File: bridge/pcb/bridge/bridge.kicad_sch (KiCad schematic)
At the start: 17 parts, among them J1 Screw_Terminal_01x06, J10 12V_Enable, J2 Screw_Terminal_01x06, J3 Screw_Terminal_01x06, J4 Conn_01x23, SW1 SW_SPST, U2 J104D2C12VDC.20S

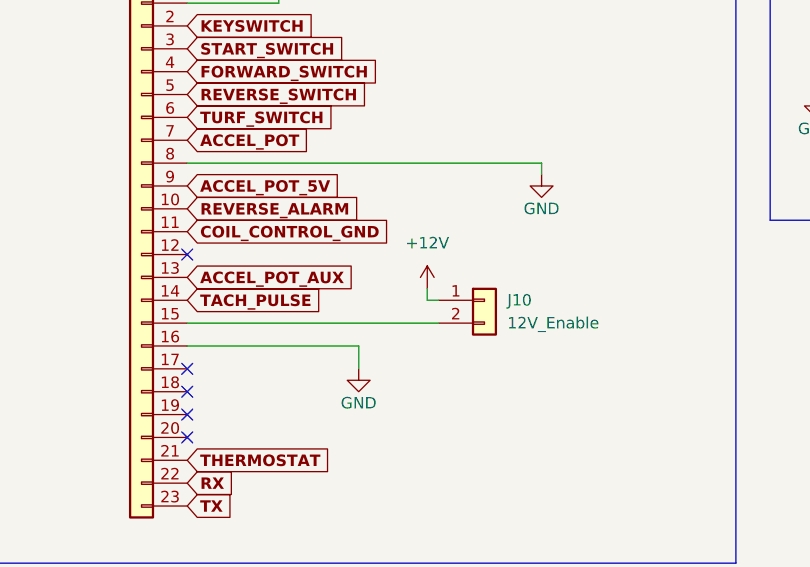
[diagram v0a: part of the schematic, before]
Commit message: Assigned footprints and layed out board
Removed 5V and 12V enable headers as they added unneeded complexity
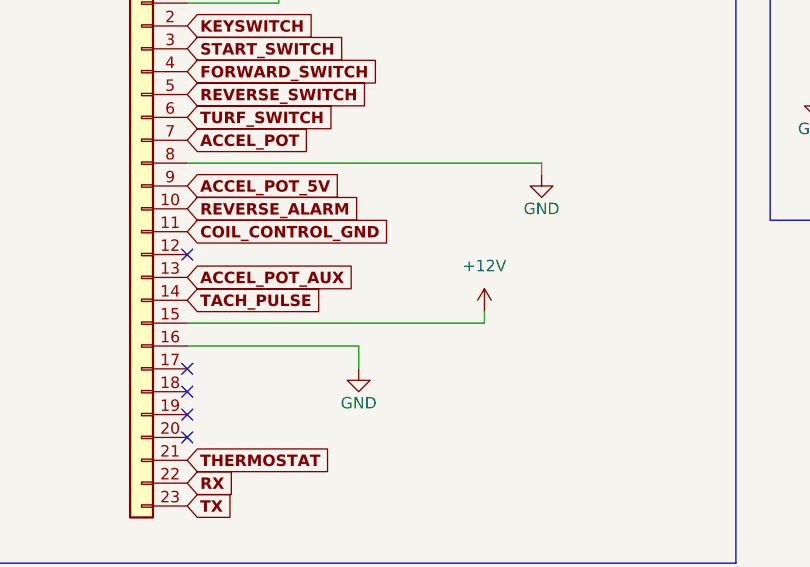
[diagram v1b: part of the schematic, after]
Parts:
- removed J10: 12V_Enable, Connector_PinHeader_2.54mm:PinHeader_1x02_P2.54mm_Vertical, symbol Connector_Generic:Conn_01x02
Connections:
- net +12V: now also J4.15 (Pin_15)
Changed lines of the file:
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@@
     (stroke (width 0) (type default))
   )
-  (wire (pts (xy 41.91 73.66) (xy 69.85 73.66))
+  (wire (pts (xy 41.91 73.66) (xy 74.93 73.66))
     (stroke (width 0) (type default))
   )
@@
     (stroke (width 0) (type default))
   )
+  (wire (pts (xy 74.93 73.66) (xy 74.93 72.39))
+    (stroke (width 0) (type default))
+  )
   (wire (pts (xy 110.49 144.78) (xy 110.49 146.05))
     (stroke (width 0) (type default))
@@
     (stroke (width 0) (type default))
   )
-  (wire (pts (xy 68.58 69.85) (xy 68.58 71.12))
-    (stroke (width 0) (type default))
-  )
   (wire (pts (xy 207.01 106.68) (xy 226.06 106.68))
     (stroke (width 0) (type default))
@@
   )
   (wire (pts (xy 153.67 91.44) (xy 153.67 93.98))
-    (stroke (width 0) (type default))
-  )
-  (wire (pts (xy 68.58 71.12) (xy 69.85 71.12))
     (stroke (width 0) (type default))
   )
@@
     )
   )
-  (symbol (lib_id "Connector_Generic:Conn_01x02") (at 74.93 71.12 0) (unit 1)
-    (in_bom yes) (on_board yes) (dnp no) (fields_autoplaced)
-    (property "Reference" "J10" (at 77.47 71.12 0)
-      (effects (font (size 1.27 1.27)) (justify left))
-    )
-    (property "Value" "12V_Enable" (at 77.47 73.66 0)
-      (effects (font (size 1.27 1.27)) (justify left))
-    )
-    (property "Footprint" "Connector_PinHeader_2.54mm:PinHeader_1x02_P2.54mm_Vertical" (at 74.93 71.12 0)
-      (effects (font (size 1.27 1.27)) hide)
-    )
-    (property "Datasheet" "~" (at 74.93 71.12 0)
-      (effects (font (size 1.27 1.27)) hide)
-    )
-    (pin "1")
-    (pin "2")
-    (instances
-      (project "bridge"
-        (path "/40a0f45e-7290-47b9-8da3-09f7dfbfbbd7"
-          (reference "J10") (unit 1)
-        )
-      )
-    )
-  )
   (symbol (lib_id "Connector:Screw_Terminal_01x06") (at 233.68 109.22 0) (unit 1)
     (in_bom yes) (on_board yes) (dnp no) (fields_autoplaced)
@@
     )
   )
-  (symbol (lib_id "power:+12V") (at 68.58 69.85 0) (unit 1)
-    (in_bom yes) (on_board yes) (dnp no) (fields_autoplaced)
-    (property "Reference" "#PWR03" (at 68.58 73.66 0)
-      (effects (font (size 1.27 1.27)) hide)
-    )
-    (property "Value" "+12V" (at 68.58 64.77 0)
-      (effects (font (size 1.27 1.27)))
-    )
-    (property "Footprint" "" (at 68.58 69.85 0)
-      (effects (font (size 1.27 1.27)) hide)
-    )
-    (property "Datasheet" "" (at 68.58 69.85 0)
-      (effects (font (size 1.27 1.27)) hide)
-    )
+  (symbol (lib_id "power:+12V") (at 74.93 72.39 0) (unit 1)
+    (in_bom yes) (on_board yes) (dnp no) (fields_autoplaced)
+    (property "Reference" "#PWR03" (at 74.93 76.2 0)
+      (effects (font (size 1.27 1.27)) hide)
+    )
+    (property "Value" "+12V" (at 74.93 67.31 0)
+      (effects (font (size 1.27 1.27)))
+    )
+    (property "Footprint" "" (at 74.93 72.39 0)
+      (effects (font (size 1.27 1.27)) hide)
+    )
+    (property "Datasheet" "" (at 74.93 72.39 0)
+      (effects (font (size 1.27 1.27)) hide)
+    )

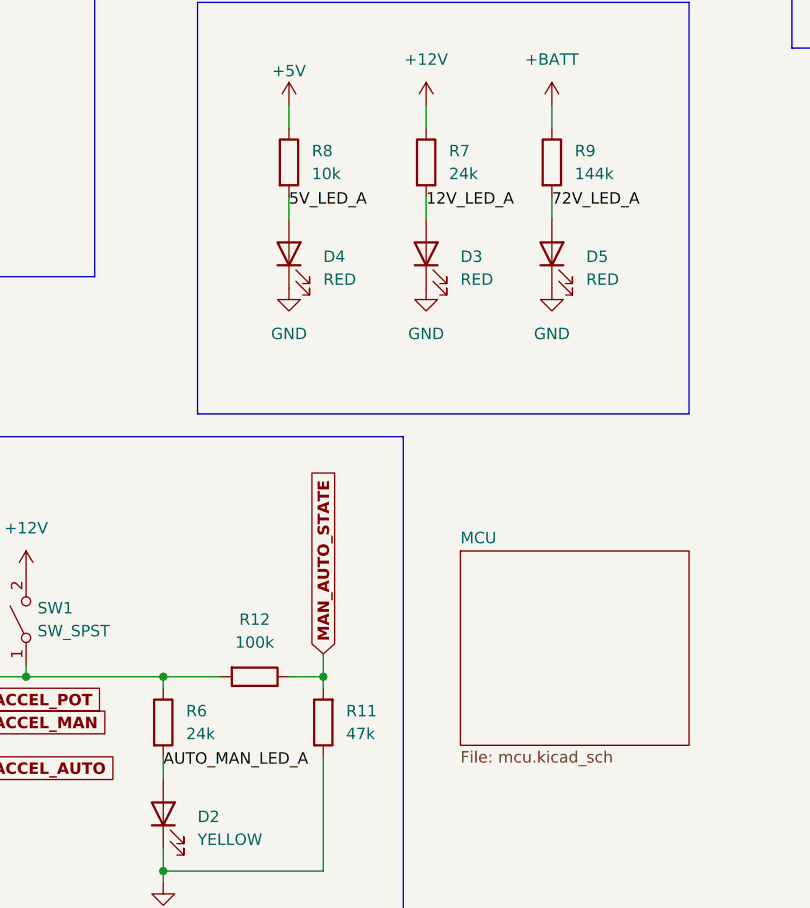
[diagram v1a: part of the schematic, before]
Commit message: Updated resistor values to make LEDs brighter
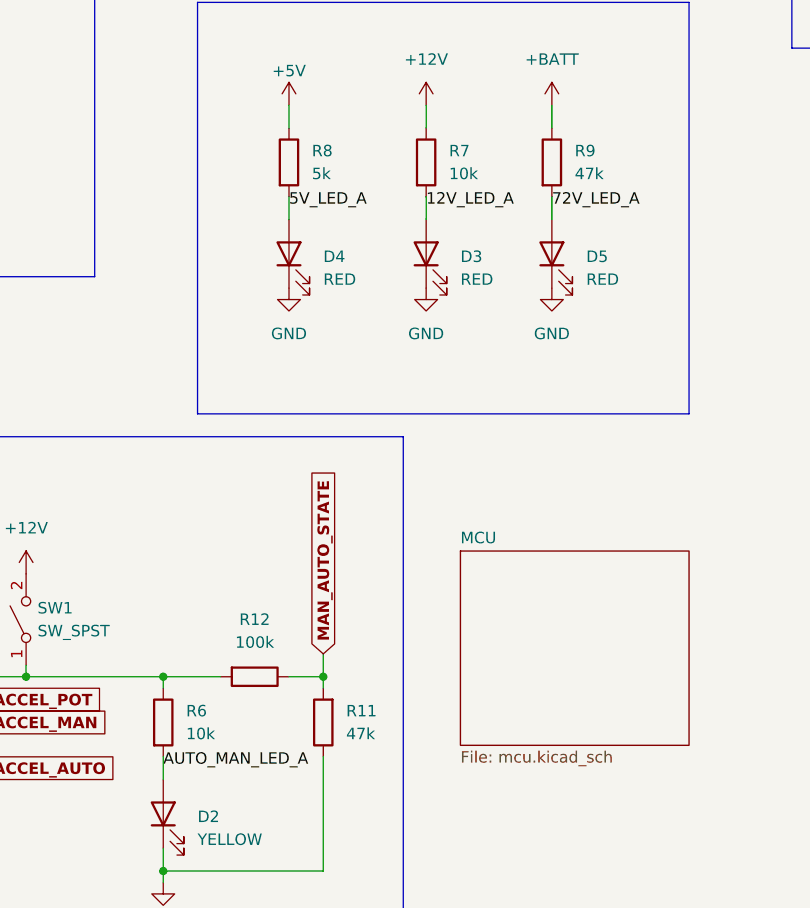
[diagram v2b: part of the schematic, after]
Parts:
- R6, R7: value 24k -> 10k
- R8: value 10k -> 5k
- R9: value 144k -> 47k
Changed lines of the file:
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@@
       (effects (font (size 1.27 1.27)) (justify left))
     )
-    (property "Value" "144k" (at 156.21 88.9 0)
+    (property "Value" "47k" (at 156.21 88.9 0)
       (effects (font (size 1.27 1.27)) (justify left))
     )
@@
       (effects (font (size 1.27 1.27)) (justify left))
     )
-    (property "Value" "10k" (at 127 88.9 0)
+    (property "Value" "5k" (at 127 88.9 0)
       (effects (font (size 1.27 1.27)) (justify left))
     )
@@
       (effects (font (size 1.27 1.27)) (justify left))
     )
-    (property "Value" "24k" (at 142.24 88.9 0)
+    (property "Value" "10k" (at 142.24 88.9 0)
       (effects (font (size 1.27 1.27)) (justify left))
     )
@@
       (effects (font (size 1.27 1.27)) (justify left))
     )
-    (property "Value" "24k" (at 113.03 151.13 0)
-      (effects (font (size 1.27 1.27)) (justify left))
-    )
+    (property "Value" "10k" (at 113.03 151.13 0)
+      (effects (font (size 1.27 1.27)) (justify left))
+    )

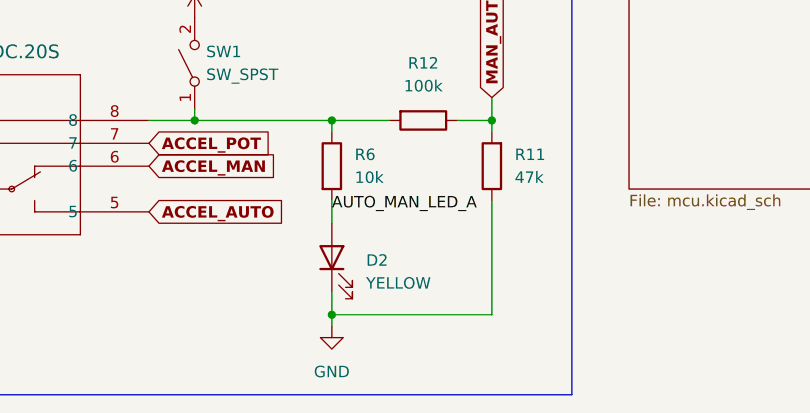
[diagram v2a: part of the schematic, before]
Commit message: Adjusted LED colors
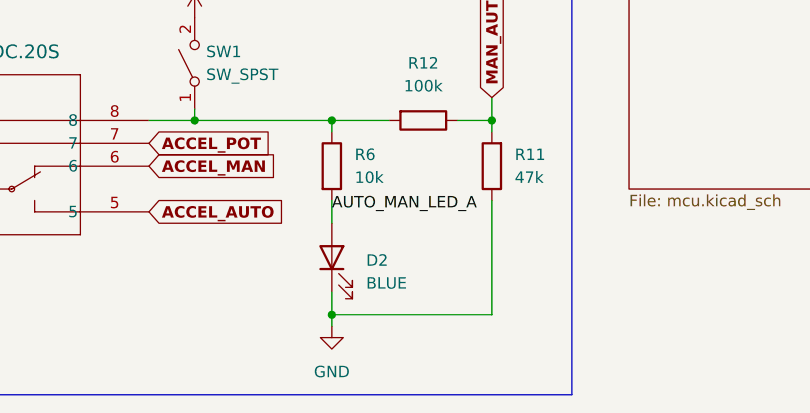
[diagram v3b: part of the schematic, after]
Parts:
- D2: value YELLOW -> BLUE
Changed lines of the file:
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@@
       (effects (font (size 1.27 1.27)) (justify right))
     )
-    (property "Value" "YELLOW" (at 114.3 162.8775 90)
+    (property "Value" "BLUE" (at 114.3 162.8775 90)
       (effects (font (size 1.27 1.27)) (justify right))
     )

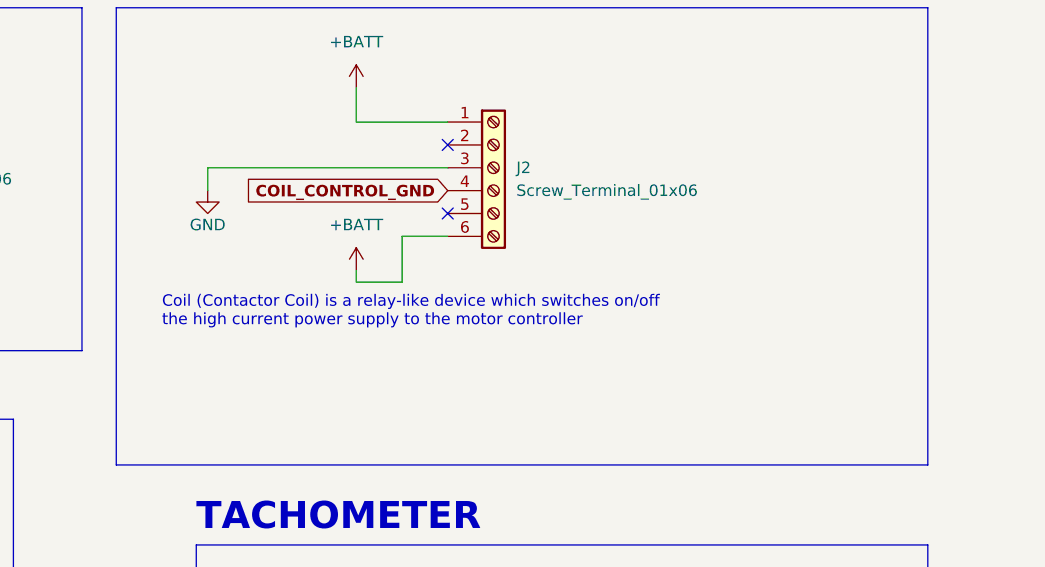
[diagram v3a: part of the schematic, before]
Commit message: Added switch for contactor coil, adjusted labeling
Slightly changed labels for the KEY and MAN/AUTO switches
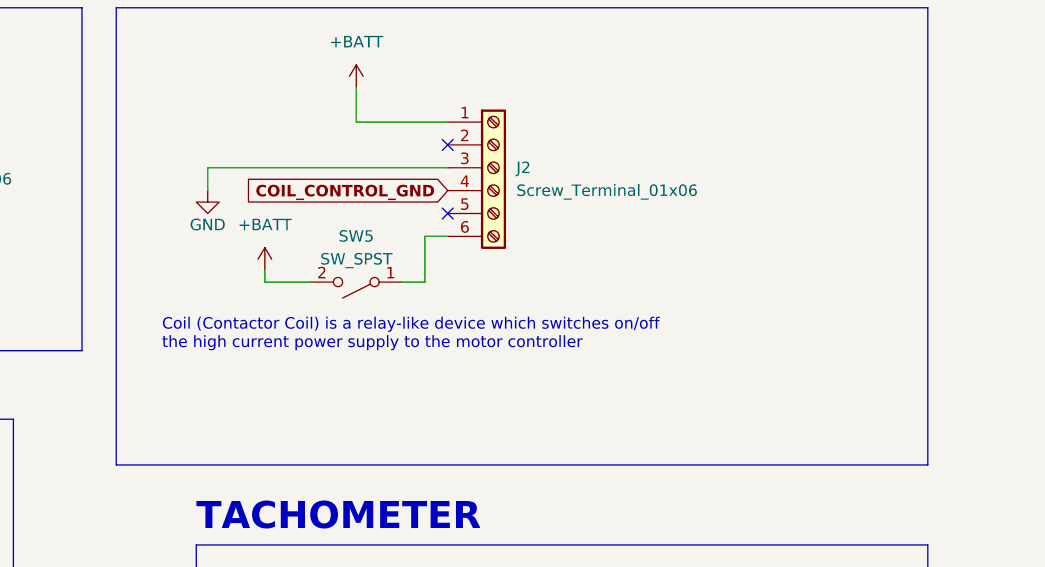
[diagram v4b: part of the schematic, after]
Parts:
- added SW5: SW_SPST, Connector_PinHeader_2.54mm:PinHeader_1x02_P2.54mm_Vertical, symbol Switch:SW_SPST
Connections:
- net +BATT: now also SW5.2 (B); no longer J2.6 (Pin_6)
- new net: J2.6 (Pin_6), SW5.1 (A)
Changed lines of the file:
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@@
     (stroke (width 0) (type default))
   )
-  (wire (pts (xy 212.09 49.53) (xy 212.09 54.61))
-    (stroke (width 0) (type default))
-  )
-  (wire (pts (xy 212.09 54.61) (xy 207.01 54.61))
+  (wire (pts (xy 201.93 54.61) (xy 196.85 54.61))
     (stroke (width 0) (type default))
   )
@@
     (stroke (width 0) (type default))
   )
+  (wire (pts (xy 214.63 49.53) (xy 217.17 49.53))
+    (stroke (width 0) (type default))
+  )
   (wire (pts (xy 95.25 144.78) (xy 110.49 144.78))
     (stroke (width 0) (type default))
@@
     (stroke (width 0) (type default))
   )
+  (wire (pts (xy 214.63 54.61) (xy 214.63 49.53))
+    (stroke (width 0) (type default))
+  )
   (wire (pts (xy 190.5 41.91) (xy 190.5 44.45))
     (stroke (width 0) (type default))
@@
     (stroke (width 0) (type default))
   )
+  (wire (pts (xy 212.09 54.61) (xy 214.63 54.61))
+    (stroke (width 0) (type default))
+  )
   (wire (pts (xy 60.96 76.2) (xy 41.91 76.2))
     (stroke (width 0) (type default))
@@
     (stroke (width 0) (type default))
   )
-  (wire (pts (xy 217.17 49.53) (xy 212.09 49.53))
-    (stroke (width 0) (type default))
-  )
   (wire (pts (xy 110.49 167.64) (xy 110.49 166.37))
     (stroke (width 0) (type default))
@@
     (stroke (width 0) (type default))
   )
-  (wire (pts (xy 207.01 54.61) (xy 207.01 53.34))
+  (wire (pts (xy 196.85 54.61) (xy 196.85 53.34))
     (stroke (width 0) (type default))
   )
@@
   )
   (text "Coil (Contactor Coil) is a relay-like device which switches on/off\nthe high current power supply to the motor controller"
-    (at 185.42 59.69 0)
+    (at 185.42 62.23 0)
     (effects (font (size 1.27 1.27)) (justify left bottom))
   )
@@
     )
   )
+  (symbol (lib_id "Switch:SW_SPST") (at 207.01 54.61 180) (unit 1)
+    (in_bom yes) (on_board yes) (dnp no) (fields_autoplaced)
+    (property "Reference" "SW5" (at 207.01 49.53 0)
+      (effects (font (size 1.27 1.27)))
+    )
+    (property "Value" "SW_SPST" (at 207.01 52.07 0)
+      (effects (font (size 1.27 1.27)))
+    )
+    (property "Footprint" "Connector_PinHeader_2.54mm:PinHeader_1x02_P2.54mm_Vertical" (at 207.01 54.61 0)
+      (effects (font (size 1.27 1.27)) hide)
+    )
+    (property "Datasheet" "~" (at 207.01 54.61 0)
+      (effects (font (size 1.27 1.27)) hide)
+    )
+    (pin "1")
+    (pin "2")
+    (instances
+      (project "bridge"
+        (path "/40a0f45e-7290-47b9-8da3-09f7dfbfbbd7"
+          (reference "SW5") (unit 1)
+        )
+      )
+    )
+  )
   (symbol (lib_id "power:GND") (at 124.46 101.6 0) (unit 1)
     (in_bom yes) (on_board yes) (dnp no) (fields_autoplaced)
@@
     )
   )
-  (symbol (lib_id "power:+BATT") (at 207.01 53.34 0) (mirror y) (unit 1)
-    (in_bom yes) (on_board yes) (dnp no) (fields_autoplaced)
-    (property "Reference" "#PWR030" (at 207.01 57.15 0)
-      (effects (font (size 1.27 1.27)) hide)
-    )
-    (property "Value" "+BATT" (at 207.01 48.26 0)
-      (effects (font (size 1.27 1.27)))
-    )
-    (property "Footprint" "" (at 207.01 53.34 0)
-      (effects (font (size 1.27 1.27)) hide)
-    )
-    (property "Datasheet" "" (at 207.01 53.34 0)
-      (effects (font (size 1.27 1.27)) hide)
-    )
+  (symbol (lib_id "power:+BATT") (at 196.85 53.34 0) (mirror y) (unit 1)
+    (in_bom yes) (on_board yes) (dnp no) (fields_autoplaced)
+    (property "Reference" "#PWR030" (at 196.85 57.15 0)
+      (effects (font (size 1.27 1.27)) hide)
+    )
+    (property "Value" "+BATT" (at 196.85 48.26 0)
+      (effects (font (size 1.27 1.27)))
+    )
+    (property "Footprint" "" (at 196.85 53.34 0)
+      (effects (font (size 1.27 1.27)) hide)
+    )
+    (property "Datasheet" "" (at 196.85 53.34 0)
+      (effects (font (size 1.27 1.27)) hide)
+    )
